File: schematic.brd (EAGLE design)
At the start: 99.6 x 134.6 mm, 94 parts, among them IC1 AD8015, IC2 AD8015, IC3 AD8015

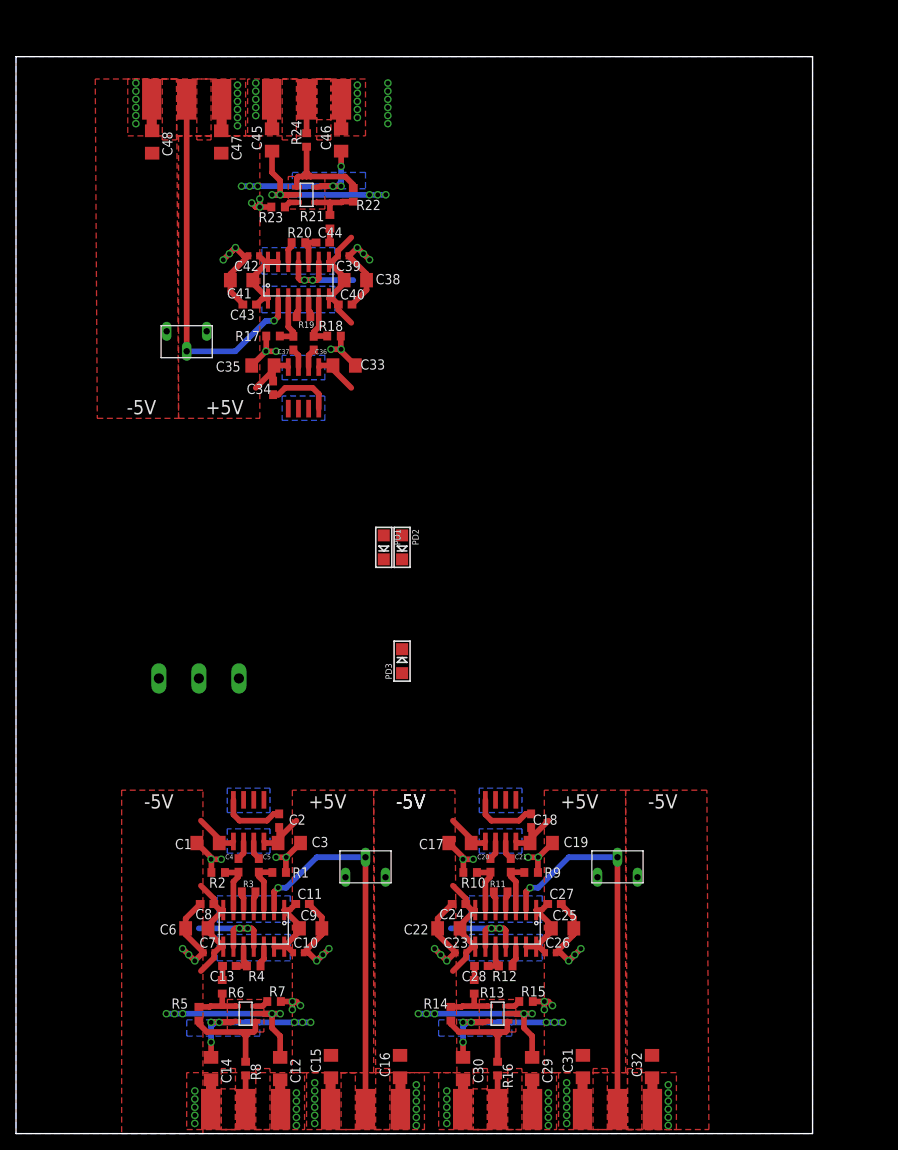
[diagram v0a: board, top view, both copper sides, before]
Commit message: Added fourth channel and lined up
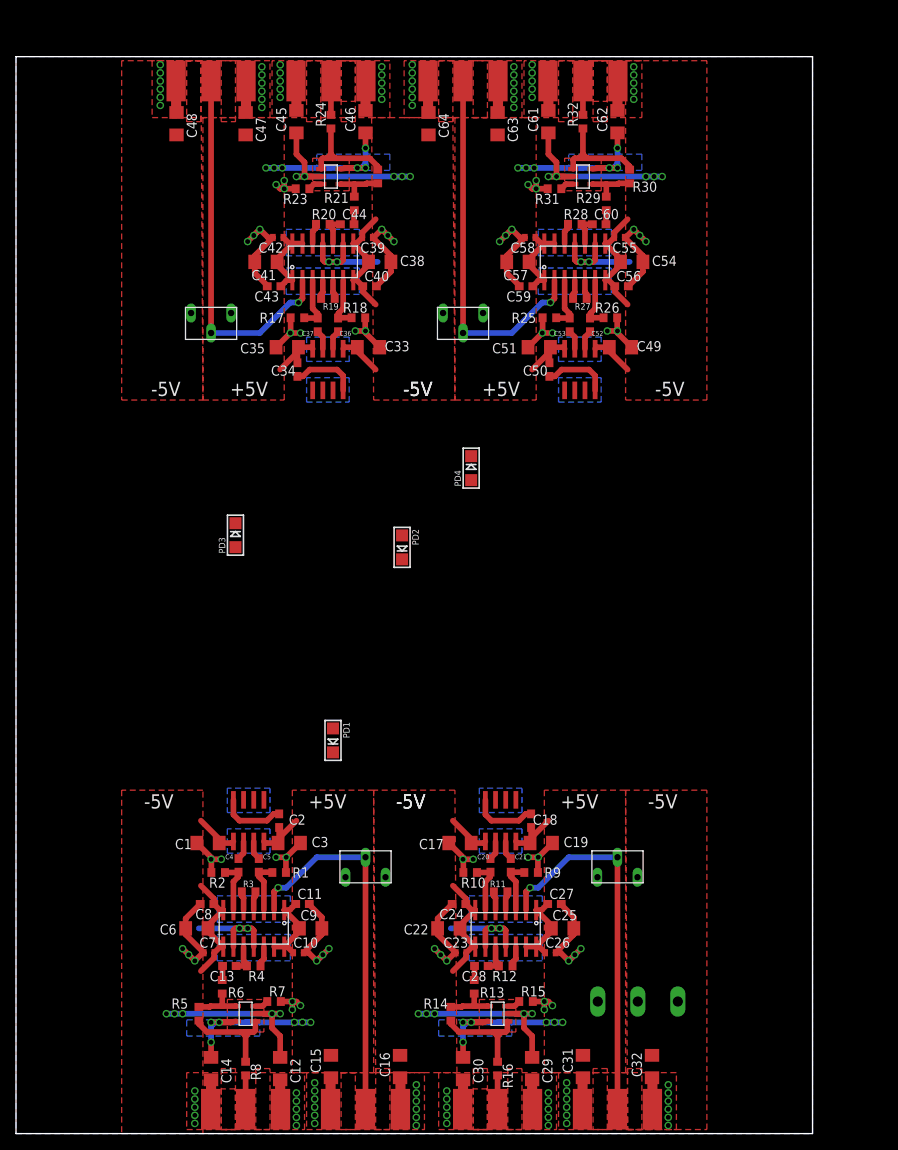
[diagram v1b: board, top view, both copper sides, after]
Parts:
- added C49, C51, C54, C57, C61, C62, C63, C64: 6.8uF, rcl:C1206
- added C50: .1uF, rcl:C0603
- added C52, C53, C60: 2.2uF, rcl:C0603
- added C55, C58: 0.1uF, rcl:C0402
- added C56, C59: 0.1uF, rcl:C0603
- added IC4: AD8015, analog-devices:SO8
- added PD4: (no value), microbuilder:CHIPLED_1206
- added R25, R26, R32: 50, rcl:R0603
- added R27: 100, rcl:R0603
- added R28: 1k, rcl:R0603
- added R29: 30, rcl:R0603
- added R30: 500, rcl:R0603
- added R31: 28, rcl:R0603
- added U$17: LMH6503, 12-ChannelEMG:SOIC14
- added U$18: PV37W, 12-ChannelEMG:PV37W
- added U$19, U$20: BNCCONN, 12-ChannelEMG:BNCPADS
- added U$21: LMH6624, 12-ChannelEMG:SOT-23
- moved U$3 68.1 mm to (77.7, 16.5)
- moved PD3 26.1 mm to (27.4, 74.8)
- moved PD1 25.0 mm to (39.6, 49.1)
- moved C33 3.81 mm to (44.1, 98.3)
- moved C34 3.81 mm to (35.2, 95.5)
- moved C36 3.81 mm to (40.3, 101.1)
- moved C37 3.81 mm to (37.7, 101.1)
- moved C39 3.81 mm to (43.9, 112.0)
- moved C43 3.81 mm to (32.3, 105.9)
- moved C44 3.81 mm to (41.4, 113.7)
- moved C45 3.81 mm to (35.1, 126.5)
- moved C46 3.81 mm to (43.7, 126.5)
- moved C47 3.81 mm to (28.7, 126.2)
- moved R17 3.81 mm to (35.2, 102.0)
- moved R18 3.81 mm to (42.8, 102.0)
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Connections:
- new net N$69: C50.2, IC4.4
- new net N$70: IC4.2, PD4.C
- new net N$71: C53.1, IC4.7
- new net N$72: C52.1, IC4.6
- new net N$73: C52.2, R26.2, U$17.6
- new net N$74: C53.2, R25.1, U$17.3
- new net N$75: R27.1, U$17.4
- new net N$76: R27.2, U$17.5
- new net N$77: R28.1, U$17.12
- new net N$78: C60.1, R28.2, U$17.10
- new net N$79: C60.2, R29.1
- new net N$80: U$17.2, U$18.2, U$19.2
- new net N$81: R29.2, R30.1, U$21.4
- new net N$82: R31.1, U$21.3
- new net N$83: R30.2, R32.1, U$21.1
- new net N$84: R32.2, U$20.2
- net +5V: now also C50.1, C51.1, C57.1, C58.1, C59.1, C62.1, C63.1, IC4.8, U$17.1, U$17.13, U$17.14, U$18.1, U$21.5
- net -5V: now also C49.1, C54.1, C55.1, C56.1, C61.1, C64.1, IC4.5, PD4.A, U$17.7, U$17.8, U$18.3, U$21.2
- net GND: now also C49.2, C51.2, C54.2, C55.2, C56.2, C57.2, C58.2, C59.2, C61.2, C62.2, C63.2, C64.2, R25.2, R26.1, R31.2, U$17.11, U$17.9, U$19.1, U$19.3, U$20.1, U$20.3
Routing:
- net GND: track 206.9 -> 275.8 mm, vias 117 -> 148
- net N$80: track 0.00 -> 46.7 mm, vias 0 -> 1
- net -5V: track 134.5 -> 179.3 mm, vias 15 -> 20
- net +5V: track 120.9 -> 161.2 mm, vias 18 -> 24
- net N$83: track 0.00 -> 14.3 mm
- net N$69: track 0.00 -> 8.22 mm
- net N$74: track 0.00 -> 6.71 mm
- net N$73: track 0.00 -> 6.65 mm
- net N$81: track 0.00 -> 6.23 mm
- net N$84: track 0.00 -> 4.23 mm
- net N$78: track 0.00 -> 3.93 mm
- net N$75: track 0.00 -> 2.88 mm
- net N$77: track 0.00 -> 2.59 mm
- net N$72: track 0.00 -> 2.40 mm
- net N$71: track 0.00 -> 2.40 mm
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- added copper zone on layer 1, net N$85
- added copper zone on layer 16, net N$85
- added copper zone on layer 1, net N$86
- added copper zone on layer 1, net N$87
- added copper zone on layer 16, net N$87
- added copper zone on layer 1, net N$88
- added copper zone on layer 1, net N$89
- added copper zone on layer 1, net N$90

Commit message: Added second power plug
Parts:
- added U$22: DIVERSITYPWR, 12-ChannelEMG:DIVERSITYPOWER
- moved PD3 21.6 mm to (48.8, 71.6)
- moved PD1 19.7 mm to (48.8, 66.5)
- moved PD4 13.1 mm to (50.8, 71.6)
- moved PD2 7.19 mm to (50.8, 66.5)
- turned U$3 to 180 degrees
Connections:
- net +5V: now also U$22.+5V
- net -5V: now also U$22.-5
- net GND: now also U$22.GND
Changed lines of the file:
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@@
 <attribute name="VALUE" x="32.893" y="33.782" size="1.27" layer="27"/>
 </element>
-<element name="PD1" library="microbuilder" package="CHIPLED_1206" value="" x="39.624" y="49.149" rot="R180"/>
+<element name="PD1" library="microbuilder" package="CHIPLED_1206" value="" x="48.768" y="66.548" rot="R180"/>
 <element name="C4" library="rcl" package="C0603" value="2.2uF" x="27.813" y="33.528" smashed="yes" rot="R270">
 <attribute name="NAME" x="26.162" y="34.29" size="0.6096" layer="25"/>
@@
 </element>
 <element name="U$2" library="12-ChannelEMG" package="PV37W" value="PV37W" x="43.688" y="34.544"/>
-<element name="U$3" library="12-ChannelEMG" package="DIVERSITYPOWER" value="DIVERSITYPWR" x="77.724" y="16.51"/>
+<element name="U$3" library="12-ChannelEMG" package="DIVERSITYPOWER" value="DIVERSITYPWR" x="77.724" y="16.51" rot="R180"/>
 <element name="U$4" library="12-ChannelEMG" package="BNCPADS" value="BNCCONN" x="43.688" y="3.048"/>
 <element name="U$5" library="12-ChannelEMG" package="BNCPADS" value="BNCCONN" x="28.702" y="3.048"/>
@@
 <attribute name="VALUE" x="64.389" y="33.782" size="1.27" layer="27"/>
 </element>
-<element name="PD2" library="microbuilder" package="CHIPLED_1206" value="" x="48.26" y="73.279" rot="R180"/>
+<element name="PD2" library="microbuilder" package="CHIPLED_1206" value="" x="50.8" y="66.548" rot="R180"/>
 <element name="C20" library="rcl" package="C0603" value="2.2uF" x="59.309" y="33.528" smashed="yes" rot="R270">
 <attribute name="NAME" x="57.658" y="34.29" size="0.6096" layer="25"/>
@@
 <attribute name="VALUE" x="35.179" y="100.838" size="1.27" layer="27" rot="R180"/>
 </element>
-<element name="PD3" library="microbuilder" package="CHIPLED_1206" value="" x="27.432" y="74.803"/>
+<element name="PD3" library="microbuilder" package="CHIPLED_1206" value="" x="48.768" y="71.628"/>
 <element name="C36" library="rcl" package="C0603" value="2.2uF" x="40.259" y="101.092" smashed="yes" rot="R90">
 <attribute name="NAME" x="41.91" y="100.33" size="0.6096" layer="25" rot="R180"/>
@@
 <attribute name="VALUE" x="66.675" y="100.838" size="1.27" layer="27" rot="R180"/>
 </element>
-<element name="PD4" library="microbuilder" package="CHIPLED_1206" value="" x="56.896" y="83.185"/>
+<element name="PD4" library="microbuilder" package="CHIPLED_1206" value="" x="50.8" y="71.628"/>
 <element name="C52" library="rcl" package="C0603" value="2.2uF" x="71.755" y="101.092" smashed="yes" rot="R90">
 <attribute name="NAME" x="73.406" y="100.33" size="0.6096" layer="25" rot="R180"/>
@@
 <attribute name="VALUE" x="54.102" y="124.968" size="1.27" layer="27" rot="R90"/>
 </element>
+<element name="U$22" library="12-ChannelEMG" package="DIVERSITYPOWER" value="DIVERSITYPWR" x="21.844" y="118.11"/>
 </elements>
 <signals>
@@
 <wire x1="47.244" y1="119.634" x2="48.26" y2="119.634" width="0.7112" layer="16"/>
 <wire x1="48.26" y1="119.634" x2="49.276" y2="119.634" width="0.7112" layer="16"/>
-<wire x1="48.26" y1="74.775" x2="56.896" y2="81.689" width="0" layer="19" extent="1-1"/>
-<wire x1="44.958" y1="95.504" x2="56.896" y2="81.689" width="0" layer="19" extent="1-1"/>
+<contactref element="U$22" pad="-5"/>
+<wire x1="48.768" y1="70.132" x2="50.8" y2="70.132" width="0" layer="19" extent="1-1"/>
+<wire x1="50.8" y1="68.044" x2="50.8" y2="70.132" width="0" layer="19" extent="1-1"/>
+<wire x1="48.768" y1="68.044" x2="50.8" y2="68.044" width="0" layer="19" extent="1-1"/>
+<wire x1="44.958" y1="95.504" x2="48.768" y2="70.132" width="0" layer="19" extent="1-1"/>
 <wire x1="66.548" y1="125.092" x2="51.562" y2="124.838" width="0" layer="19" extent="1-1"/>
 <wire x1="20.066" y1="124.838" x2="35.052" y2="125.092" width="0" layer="19" extent="1-1"/>
-<wire x1="27.432" y1="73.307" x2="48.26" y2="74.775" width="0" layer="19" extent="1-1"/>
-<wire x1="72.7202" y1="16.51" x2="27.432" y2="73.307" width="0" layer="19" extent="1-1"/>
-<wire x1="23.114" y1="39.116" x2="72.7202" y2="16.51" width="0" layer="19" extent="1-1"/>
-<wire x1="48.006" y1="9.782" x2="33.02" y2="9.528" width="0" layer="19" extent="1-1"/>
+<wire x1="54.61" y1="39.116" x2="50.8" y2="68.044" width="0" layer="19" extent="1-1"/>
 <wire x1="79.502" y1="9.782" x2="64.516" y2="9.528" width="0" layer="19" extent="1-1"/>
-<wire x1="39.624" y1="50.645" x2="27.178" y2="36.516" width="0" layer="19" extent="1-1"/>
+<wire x1="33.02" y1="9.528" x2="48.006" y2="9.782" width="0" layer="19" extent="1-1"/>
 </signal>
 <signal name="+5V">
@@
 <wire x1="75.184" y1="121.158" x2="75.1205" y2="121.158" width="0.7112" layer="16"/>
 <wire x1="75.1205" y1="121.158" x2="74.676" y2="120.7135" width="0.7112" layer="16"/>
-<wire x1="35.052" y1="39.116" x2="82.7278" y2="16.51" width="0" layer="19" extent="1-1"/>
-<wire x1="55.88" y1="9.528" x2="39.37" y2="9.782" width="0" layer="19" extent="1-1"/>
-<wire x1="33.02" y1="95.504" x2="82.7278" y2="16.51" width="0" layer="19" extent="1-1"/>
-<wire x1="60.198" y1="124.838" x2="43.688" y2="125.092" width="0" layer="19" extent="1-1"/>
+<contactref element="U$22" pad="+5V"/>
+<wire x1="43.688" y1="125.092" x2="60.198" y2="124.838" width="0" layer="19" extent="1-1"/>
+<wire x1="66.548" y1="39.116" x2="64.516" y2="95.504" width="0" layer="19" extent="1-1"/>
+<wire x1="39.37" y1="9.782" x2="55.88" y2="9.528" width="0" layer="19" extent="1-1"/>
 </signal>
 <signal name="N$3">
@@
 <contactref element="PD1" pad="C"/>
 <contactref element="IC1" pad="2"/>
-<wire x1="29.718" y1="41.716" x2="39.624" y2="47.653" width="0" layer="19" extent="1-1"/>
+<wire x1="29.718" y1="41.716" x2="48.768" y2="65.052" width="0" layer="19" extent="1-1"/>
 </signal>
 <signal name="N$2">
@@
 <wire x1="66.548" y1="127.892" x2="66.548" y2="129.9972" width="1.27" layer="1"/>
 <wire x1="66.548" y1="129.9972" x2="66.4972" y2="130.048" width="1.27" layer="1"/>
+<contactref element="U$22" pad="GND"/>
 </signal>
 <signal name="N$19">
@@
 <contactref element="PD2" pad="C"/>
 <contactref element="IC2" pad="2"/>
-<wire x1="61.214" y1="41.716" x2="48.26" y2="71.783" width="0" layer="19" extent="1-1"/>
+<wire x1="61.214" y1="41.716" x2="50.8" y2="65.052" width="0" layer="19" extent="1-1"/>
 </signal>
 <signal name="N$27">
@@
 <contactref element="PD3" pad="C"/>
 <contactref element="IC3" pad="2"/>
-<wire x1="27.432" y1="76.299" x2="38.354" y2="92.904" width="0" layer="19" extent="1-1"/>
+<wire x1="48.768" y1="73.124" x2="38.354" y2="92.904" width="0" layer="19" extent="1-1"/>
 </signal>
 <signal name="N$49">
@@
 <contactref element="PD4" pad="C"/>
 <contactref element="IC4" pad="2"/>
-<wire x1="56.896" y1="84.681" x2="69.85" y2="92.904" width="0" layer="19" extent="1-1"/>
+<wire x1="50.8" y1="73.124" x2="69.85" y2="92.904" width="0" layer="19" extent="1-1"/>
 </signal>
 <signal name="N$71">

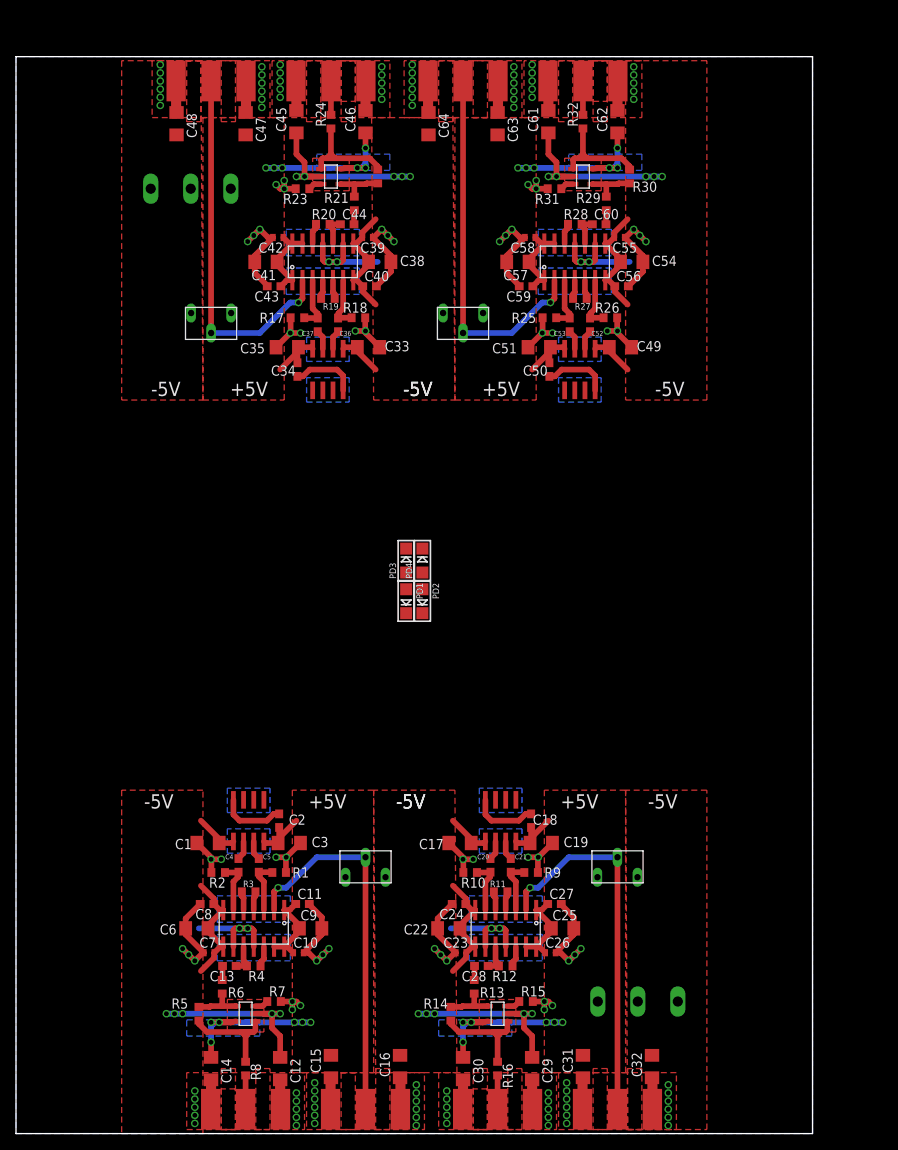
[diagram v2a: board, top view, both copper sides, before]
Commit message: Initial Silkscreen and photodiode layout with some initial power plane connections
needs fixing, some unresolved problems
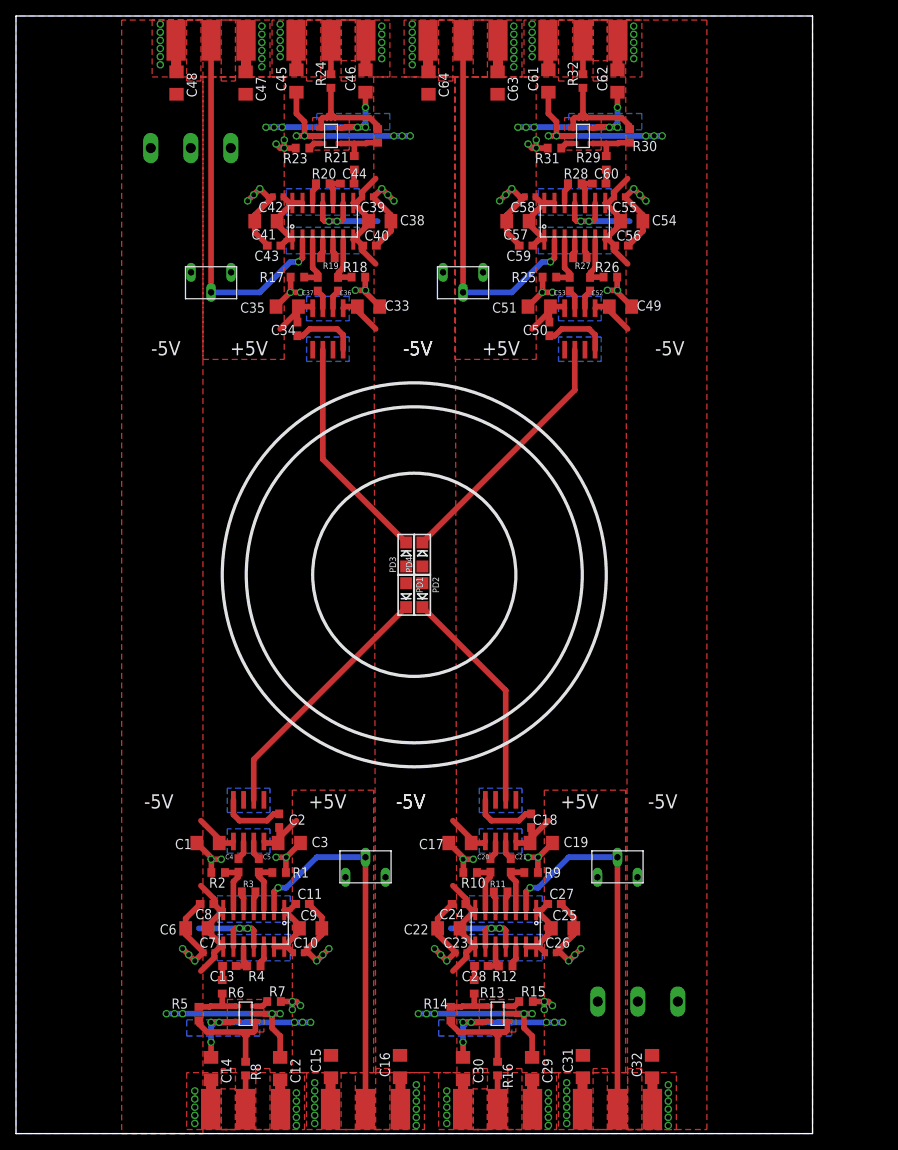
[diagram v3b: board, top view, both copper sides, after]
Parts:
- moved C38 5.08 mm to (45.5, 114.0)
- moved C41 5.08 mm to (31.2, 114.0)
- moved C47 5.08 mm to (28.7, 131.3)
- moved C48 5.08 mm to (20.1, 131.3)
- moved C54 5.08 mm to (77.0, 114.0)
- moved C57 5.08 mm to (62.7, 114.0)
- moved C63 5.08 mm to (60.2, 131.3)
- moved C64 5.08 mm to (51.6, 131.3)
- moved R17 5.08 mm to (35.2, 107.1)
- moved R18 5.08 mm to (42.8, 107.1)
- moved R25 5.08 mm to (66.7, 107.1)
- moved R26 5.08 mm to (74.3, 107.1)
- moved U$12 5.08 mm to (38.4, 114.0)
- moved U$13 5.08 mm to (24.4, 105.2)
- moved U$17 5.08 mm to (69.8, 114.0)
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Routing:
- net N$1: track 0.00 -> 32.0 mm
- net N$70: track 0.00 -> 32.0 mm
- net N$48: track 0.00 -> 28.4 mm
- net N$26: track 0.00 -> 28.4 mm
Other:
- board size 99.6 x 134.6 mm -> 99.6 x 139.7 mm

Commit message: Realigned top and bottom to optimize photodiode trace length
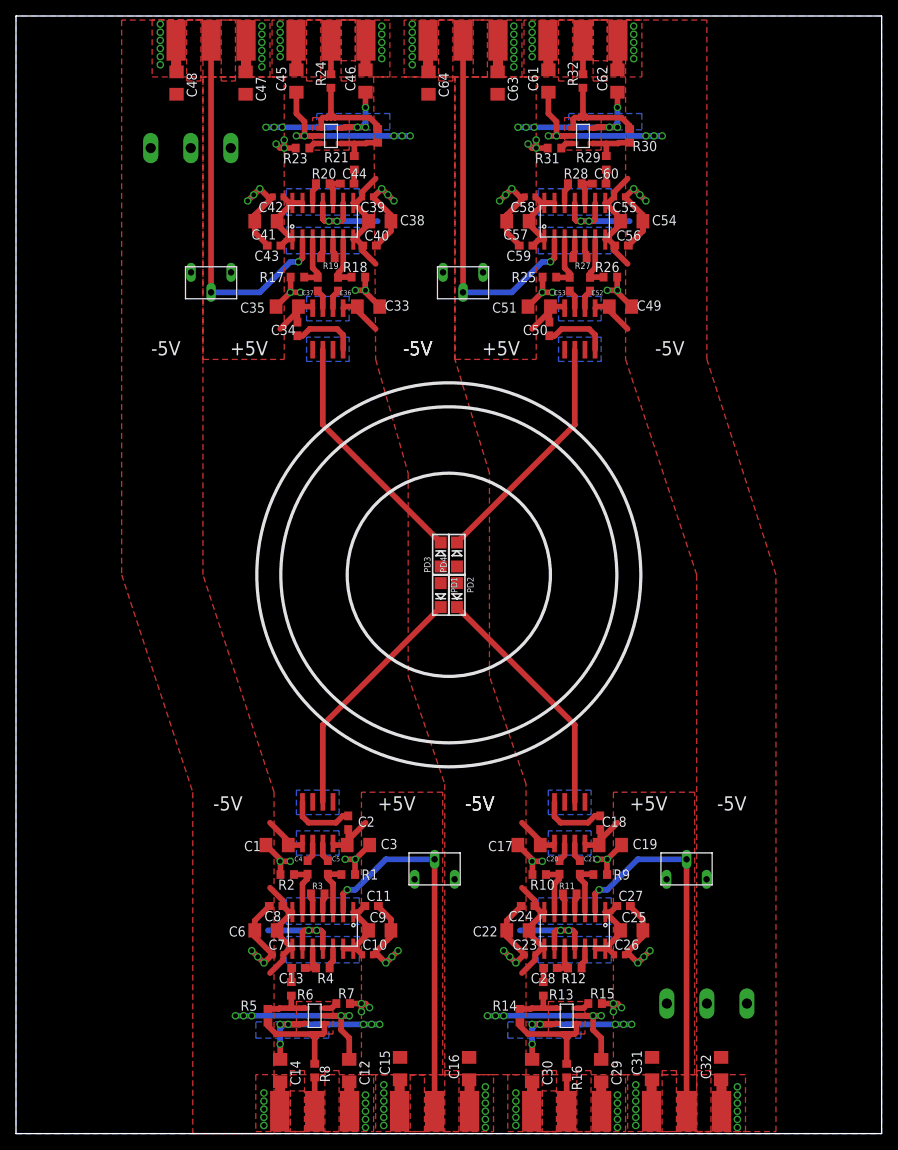
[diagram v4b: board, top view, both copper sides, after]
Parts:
- moved C18 8.64 mm to (73.0, 38.9)
- moved C25 8.64 mm to (77.0, 25.4)
- moved C28 8.64 mm to (66.8, 20.7)
- moved C32 8.64 mm to (88.1, 8.13)
- moved R9 8.64 mm to (73.0, 32.4)
- moved C1 8.64 mm to (32.6, 36.1)
- moved C10 8.64 mm to (43.9, 22.4)
- moved C11 8.64 mm to (44.5, 28.4)
- moved C14 8.64 mm to (33.0, 7.87)
- moved C15 8.64 mm to (48.0, 8.13)
- moved C16 8.64 mm to (56.6, 8.13)
- moved C17 8.64 mm to (64.1, 36.1)
- moved C2 8.64 mm to (41.5, 38.9)
- moved C21 8.64 mm to (70.5, 33.3)
- moved C22 8.64 mm to (62.7, 25.4)
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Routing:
- net N$26: track 28.4 -> 30.5 mm
- net N$70: track 32.0 -> 30.2 mm
- net N$48: track 28.4 -> 30.2 mm
- net N$1: track 32.0 -> 30.5 mm
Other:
- board size 99.6 x 139.7 mm -> 108.2 x 139.7 mm
